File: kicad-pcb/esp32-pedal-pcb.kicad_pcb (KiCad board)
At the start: 4 copper layers, 216 x 25 mm, 42 parts, among them J1 USB_C_Receptacle_USB2.0_14P, Q1 Q_PMOS_GSD, U1 MCP73871, U2 TLV75733PDBV, U3 ESP32-S3-WROOM-1, U4 TPD2EUSB30, U5 TPD2E2U06DCK, U6 TPS2553DBVR

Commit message: Update PCB documentation images and layout
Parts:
- turned D2 to 180 degrees
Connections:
- net /BAT SWITCHED renamed /5V SWITCHED
- D2 pad 1: /GND -> /VBUS PROTECTED
- D2 pad 2: /VBUS PROTECTED -> /GND

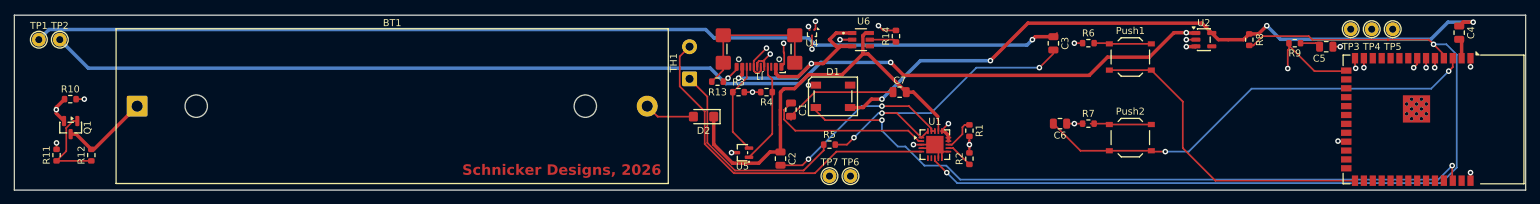
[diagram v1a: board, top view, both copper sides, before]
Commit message: Update PCB schematic and layout files
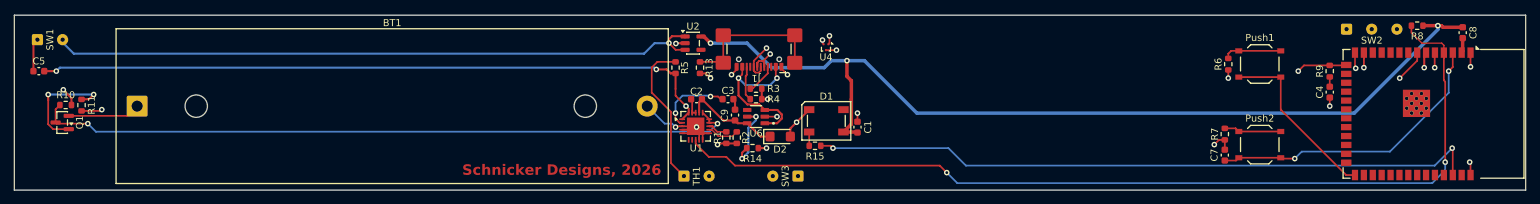
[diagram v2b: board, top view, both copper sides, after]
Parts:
- removed C6: 1µF, Capacitor_SMD:C_0805_2012Metric
- removed R12: 100kΩ, Resistor_SMD:R_0603_1608Metric
- removed TP1, TP2, TP3, TP4, TP5, TP6, TP7: TestPoint_Small, TestPoint:TestPoint_THTPad_D2.0mm_Drill1.0mm
- removed U5: TPD2E2U06DCK, Package_TO_SOT_SMD:SOT-323_SC-70
- added C8: 100µF, Capacitor_SMD:C_0603_1608Metric, F.Cu at (240.5, 90.0)
- added C9: 10µF, Capacitor_SMD:C_0603_1608Metric, F.Cu at (136.5, 101.8)
- added R15: 300Ω, Resistor_SMD:R_0603_1608Metric, F.Cu at (147.9, 106.2)
- added SW1: SW_SPST, Connector_Wire:SolderWire-0.1sqmm_1x02_P3.6mm_D0.4mm_OD1mm, F.Cu at (36.8, 91.0)
- added SW2: SW_SPDT, Connector_Wire:SolderWire-0.1sqmm_1x03_P3.6mm_D0.4mm_OD1mm, F.Cu at (223.9, 89.5)
- added SW3: SW_SPST, Connector_Wire:SolderWire-0.1sqmm_1x02_P3.6mm_D0.4mm_OD1mm, F.Cu at (145.5, 110.5)
- C1: footprint Capacitor_SMD:C_0805_2012Metric -> Capacitor_SMD:C_0603_1608Metric
- C2: value 1µF -> 47µF; footprint Capacitor_SMD:C_0805_2012Metric -> Capacitor_SMD:C_0603_1608Metric
- C3: value 47µF -> 0.1µF; footprint Capacitor_SMD:C_0805_2012Metric -> Capacitor_SMD:C_0603_1608Metric
- C4: value 100µF -> 0.1µF; footprint Capacitor_SMD:C_0805_2012Metric -> Capacitor_SMD:C_0603_1608Metric
- C5: value 0.1µF -> 47µF; footprint Capacitor_SMD:C_0805_2012Metric -> Capacitor_SMD:C_0603_1608Metric
- C7: value 10µF -> 1µF; footprint Capacitor_SMD:C_0805_2012Metric -> Capacitor_SMD:C_0603_1608Metric
- TH1: value Thermistor_NTC_US -> Thermistor; footprint Connector_Wire:SolderWire-0.5sqmm_1x02_P4.6mm_D0.9mm_OD2.1mm -> Connector_Wire:SolderWire-0.1sqmm_1x02_P3.6mm_D0.4mm_OD1mm
- moved C5 184.0 mm to (37.0, 95.5), turned to 0 degrees
- moved U2 73.0 mm to (130.5, 91.5)
- moved C7 47.3 mm to (206.5, 107.5), turned to -90 degrees
- moved C3 47.2 mm to (135.5, 99.5), turned to 180 degrees
- moved R1 34.8 mm to (135.2, 105.0)
- moved U1 34.3 mm to (130.9, 103.4)
- moved R2 33.4 mm to (136.8, 105.0), turned to -90 degrees
- moved R14 26.0 mm to (139.0, 106.5), turned to 0 degrees
- moved R5 24.6 mm to (128.0, 95.0), turned to -90 degrees
- moved R8 24.1 mm to (234.0, 89.0), turned to 180 degrees
- moved C4 20.4 mm to (221.5, 98.5), turned to 90 degrees
- moved R6 20.2 mm to (207.0, 94.5), turned to 90 degrees
- moved R7 19.6 mm to (206.5, 104.5), turned to 90 degrees
- moved U6 18.6 mm to (139.5, 102.0), turned to 180 degrees
- moved Push1 18.5 mm to (211.5, 94.5)
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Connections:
- net /5V SWITCHED renamed /MCP OUT 5V SWITCHED
- BT1 pad 1: /BAT -> /BAT+
- BT1 pad 2: /GND -> GND
- C1 pad 1: Net-(U1-VPCC) -> GND
- C1 pad 2: Net-(C1-Pad2) -> unconnected-(C1-Pad2)
- C2 pad 1: /VBUS PROTECTED -> Net-(C2-Pad1)
- C2 pad 2: Net-(C2-Pad2) -> /VBUS P
- C3 pad 2: Net-(C3-Pad2) -> Net-(U1-VPCC)
- C4 pad 1: /3V3 -> GND
- C4 pad 2: Net-(U3-3V3) -> Net-(C4-Pad2)
- C5 pad 1: /GND -> Net-(SW1-A)
- C5 pad 2: Net-(C5-Pad2) -> /MCP OUT 5V
- C7 pad 1: Net-(C1-Pad2) -> GND
- C7 pad 2: /VBUS PROTECTED -> /RESET
- D1 pad 1: /GND -> GND
- D1 pad 2: /Led DIN -> Net-(D1-DIN)
- D1 pad 3: /3V3 -> GND
- D2 pad 1: /VBUS PROTECTED -> /VBUS P
- D2 pad 2: /GND -> GND
- J1 pad A1: /GND -> GND
- J1 pad A12: /GND -> GND
- J1 pad B1: /GND -> GND
- J1 pad B12: /GND -> GND
- Q1 pad 2: /VBAT -> /BAT+
- Q1 pad 3: /BAT -> Net-(Q1-D)
- R1 pad 2: /GND -> GND
- R10 pad 1: /VBAT -> Net-(Q1-D)
- R11 pad 2: /GND -> GND
- R13 pad 2: /GND -> GND
- R14 pad 2: /GND -> GND
- R2 pad 2: /GND -> GND
- R3 pad 1: Net-(J1-CC2) -> Net-(J1-CC1)
- R3 pad 2: /GND -> GND
- R4 pad 1: Net-(J1-CC1) -> Net-(J1-CC2)
- R4 pad 2: /GND -> GND
- R5 pad 2: Net-(C3-Pad2) -> /MCP OUT 5V
- R6 pad 1: /GND -> GND
- R7 pad 1: /GND -> GND
- R8 pad 1: /3V3 -> GND
- R9 pad 1: Net-(C5-Pad2) -> Net-(C4-Pad2)
- TH1 pad 2: Net-(U1-THERM) -> GND
- U1 pad 1: Net-(C3-Pad2) -> /MCP OUT 5V
- U1 pad 10: /GND -> GND
- U1 pad 11: /GND -> GND
- U1 pad 14: /VBAT -> Net-(Q1-D)
- U1 pad 15: /VBAT -> Net-(Q1-D)
- U1 pad 16: /VBAT -> Net-(Q1-D)
- U1 pad 17: /VBUS PROTECTED -> /VBUS P
- U1 pad 18: Net-(C2-Pad2) -> Net-(C2-Pad1)
- U1 pad 19: Net-(C2-Pad2) -> Net-(C2-Pad1)
- U1 pad 20: Net-(C3-Pad2) -> /MCP OUT 5V
- U1 pad 21: /GND -> GND
- U1 pad 3: /GND -> GND
- U1 pad 4: /GND -> GND
- U1 pad 5: Net-(U1-THERM) -> GND
- U1 pad 9: /GND -> GND
- U2 pad 2: /GND -> GND
- U2 pad 5: /3V3 -> GND
- U3 pad 1: /GND -> GND
- U3 pad 2: Net-(U3-3V3) -> GND
- U3 pad 23: Net-(U3-GPIO21) -> unconnected-(U3-GPIO21-Pad23)
- U3 pad 40: /GND -> GND
- U3 pad 41: /GND -> GND
- U3 pad 6: /GND -> Net-(SW2-A)
- U4 pad 3: /GND -> GND
- U6 pad 2: /GND -> GND
- U6 pad 6: /VBUS PROTECTED -> /VBUS P
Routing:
- net GND: track 0.00 -> 193.5 mm, vias 0 -> 21
- net Net-(C3-Pad1): track 147.8 -> 1.98 mm, vias 1 -> 0
- net /VBAT: track 136.7 -> 0.00 mm, vias 2 -> 0
- net Net-(Q1-D): track 0.00 -> 101.4 mm, vias 0 -> 2
- net /3V3: track 100.6 -> 0.00 mm, vias 4 -> 0
- net /MCP OUT 5V: track 0.00 -> 98.5 mm, vias 0 -> 3
- net Net-(SW3-A): track 8.30 -> 96.6 mm
- net /MCP OUT 5V SWITCHED: track 173.8 -> 94.1 mm, vias 3 -> 1
- net Net-(U3-GPIO21): track 75.4 -> 0.00 mm, vias 1 -> 0
- net /VBUS PROTECTED: track 58.2 -> 0.00 mm
- net /GND: track 53.5 -> 0.00 mm, vias 18 -> 0
- net Net-(U1-THERM): track 49.9 -> 0.00 mm
- net Net-(C3-Pad2): track 45.0 -> 0.00 mm, vias 3 -> 0
- net Net-(C2-Pad2): track 27.3 -> 0.00 mm, vias 2 -> 0
- net /RESET: track 65.2 -> 41.5 mm
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- added copper zone on In2.Cu, net GND
- removed copper zone on In2.Cu, net /GND
